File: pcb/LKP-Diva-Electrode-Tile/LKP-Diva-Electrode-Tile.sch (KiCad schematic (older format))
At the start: 19 parts, among them J1 Intercon, J10 Electrode 1, J11 Electrode 3, J12 Electrode 5, J13 Electrode 7, J14 Electrode 9, J15 Electrode 11, J16 Electrode 13, J17 Electrode 15, J2 Electrode 0, J3 Electrode 2, J4 Electrode 4, J5 Electrode 6, J6 Electrode 8, J7 Electrode 10, J8 Electrode 12, J9 Electrode 14

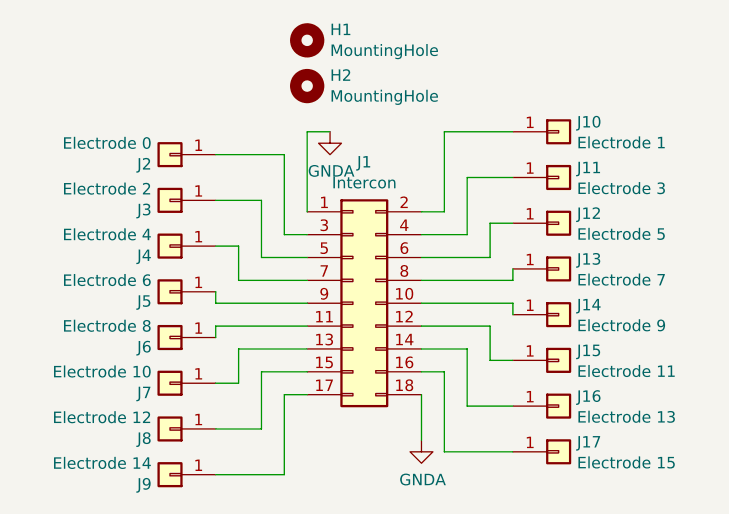
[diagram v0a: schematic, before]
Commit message: Fix sensor topology
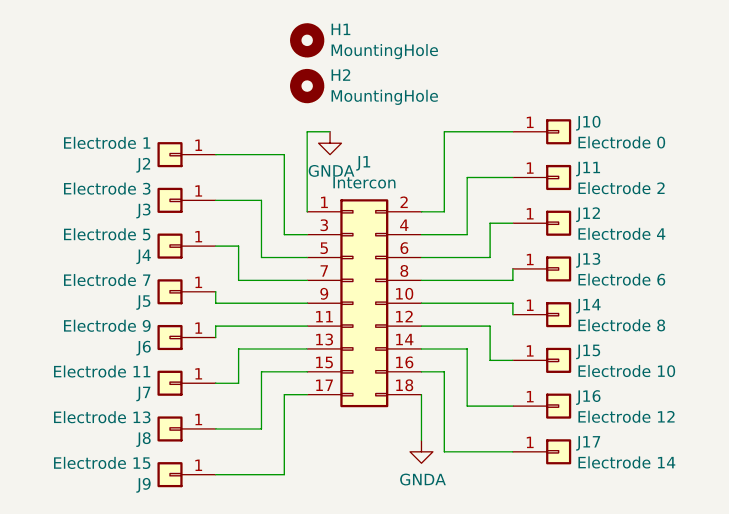
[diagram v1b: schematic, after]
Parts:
- J10: value Electrode 1 -> Electrode 0
- J11: value Electrode 3 -> Electrode 2
- J12: value Electrode 5 -> Electrode 4
- J13: value Electrode 7 -> Electrode 6
- J14: value Electrode 9 -> Electrode 8
- J15: value Electrode 11 -> Electrode 10
- J16: value Electrode 13 -> Electrode 12
- J17: value Electrode 15 -> Electrode 14
- J2: value Electrode 0 -> Electrode 1
- J3: value Electrode 2 -> Electrode 3
- J4: value Electrode 4 -> Electrode 5
- J5: value Electrode 6 -> Electrode 7
- J6: value Electrode 8 -> Electrode 9
- J7: value Electrode 10 -> Electrode 11
- J8: value Electrode 12 -> Electrode 13
- J9: value Electrode 14 -> Electrode 15
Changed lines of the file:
@@
 P 6900 3700
 F 0 "J10" H 6980 3742 50  0000 L CNN
-F 1 "Electrode 1" H 6980 3651 50  0000 L CNN
+F 1 "Electrode 0" H 6980 3651 50  0000 L CNN
 F 2 "private:CapSense_Electrode_14x38mm" H 6900 3700 50  0001 C CNN
 F 3 "~" H 6900 3700 50  0001 C CNN
@@
 P 6900 3900
 F 0 "J11" H 6980 3942 50  0000 L CNN
-F 1 "Electrode 3" H 6980 3851 50  0000 L CNN
+F 1 "Electrode 2" H 6980 3851 50  0000 L CNN
 F 2 "private:CapSense_Electrode_14x38mm" H 6900 3900 50  0001 C CNN
 F 3 "~" H 6900 3900 50  0001 C CNN
@@
 P 6900 4100
 F 0 "J12" H 6980 4142 50  0000 L CNN
-F 1 "Electrode 5" H 6980 4051 50  0000 L CNN
+F 1 "Electrode 4" H 6980 4051 50  0000 L CNN
 F 2 "private:CapSense_Electrode_14x38mm" H 6900 4100 50  0001 C CNN
 F 3 "~" H 6900 4100 50  0001 C CNN
@@
 P 6900 4300
 F 0 "J13" H 6980 4342 50  0000 L CNN
-F 1 "Electrode 7" H 6980 4251 50  0000 L CNN
+F 1 "Electrode 6" H 6980 4251 50  0000 L CNN
 F 2 "private:CapSense_Electrode_14x38mm" H 6900 4300 50  0001 C CNN
 F 3 "~" H 6900 4300 50  0001 C CNN
@@
 P 6900 4500
 F 0 "J14" H 6980 4542 50  0000 L CNN
-F 1 "Electrode 9" H 6980 4451 50  0000 L CNN
+F 1 "Electrode 8" H 6980 4451 50  0000 L CNN
 F 2 "private:CapSense_Electrode_14x38mm" H 6900 4500 50  0001 C CNN
 F 3 "~" H 6900 4500 50  0001 C CNN
@@
 P 6900 4700
 F 0 "J15" H 6980 4742 50  0000 L CNN
-F 1 "Electrode 11" H 6980 4651 50  0000 L CNN
+F 1 "Electrode 10" H 6980 4651 50  0000 L CNN
 F 2 "private:CapSense_Electrode_14x38mm" H 6900 4700 50  0001 C CNN
 F 3 "~" H 6900 4700 50  0001 C CNN
@@
 P 6900 4900
 F 0 "J16" H 6980 4942 50  0000 L CNN
-F 1 "Electrode 13" H 6980 4851 50  0000 L CNN
+F 1 "Electrode 12" H 6980 4851 50  0000 L CNN
 F 2 "private:CapSense_Electrode_14x38mm" H 6900 4900 50  0001 C CNN
 F 3 "~" H 6900 4900 50  0001 C CNN
@@
 P 6900 5100
 F 0 "J17" H 6980 5142 50  0000 L CNN
-F 1 "Electrode 15" H 6980 5051 50  0000 L CNN
+F 1 "Electrode 14" H 6980 5051 50  0000 L CNN
 F 2 "private:CapSense_Electrode_14x38mm" H 6900 5100 50  0001 C CNN
 F 3 "~" H 6900 5100 50  0001 C CNN
@@
 P 5200 4800
 F 0 "J7" H 5280 4842 50  0000 L CNN
-F 1 "Electrode 10" H 5280 4751 50  0000 L CNN
+F 1 "Electrode 11" H 5280 4751 50  0000 L CNN
 F 2 "private:CapSense_Electrode_14x38mm" H 5200 4800 50  0001 C CNN
 F 3 "~" H 5200 4800 50  0001 C CNN
@@
 P 5200 5200
 F 0 "J9" H 5280 5242 50  0000 L CNN
-F 1 "Electrode 14" H 5280 5151 50  0000 L CNN
+F 1 "Electrode 15" H 5280 5151 50  0000 L CNN
 F 2 "private:CapSense_Electrode_14x38mm" H 5200 5200 50  0001 C CNN
 F 3 "~" H 5200 5200 50  0001 C CNN
@@
 P 5200 4000
 F 0 "J3" H 5280 4042 50  0000 L CNN
-F 1 "Electrode 2" H 5280 3951 50  0000 L CNN
+F 1 "Electrode 3" H 5280 3951 50  0000 L CNN
 F 2 "private:CapSense_Electrode_14x38mm" H 5200 4000 50  0001 C CNN
 F 3 "~" H 5200 4000 50  0001 C CNN
@@
 P 5200 4400
 F 0 "J5" H 5280 4442 50  0000 L CNN
-F 1 "Electrode 6" H 5280 4351 50  0000 L CNN
+F 1 "Electrode 7" H 5280 4351 50  0000 L CNN
 F 2 "private:CapSense_Electrode_14x38mm" H 5200 4400 50  0001 C CNN
 F 3 "~" H 5200 4400 50  0001 C CNN
@@
 P 5200 4600
 F 0 "J6" H 5280 4642 50  0000 L CNN
-F 1 "Electrode 8" H 5280 4551 50  0000 L CNN
+F 1 "Electrode 9" H 5280 4551 50  0000 L CNN
 F 2 "private:CapSense_Electrode_14x38mm" H 5200 4600 50  0001 C CNN
 F 3 "~" H 5200 4600 50  0001 C CNN
@@
 P 5200 3800
 F 0 "J2" H 5280 3842 50  0000 L CNN
-F 1 "Electrode 0" H 5280 3751 50  0000 L CNN
+F 1 "Electrode 1" H 5280 3751 50  0000 L CNN
 F 2 "private:CapSense_Electrode_14x38mm" H 5200 3800 50  0001 C CNN
 F 3 "~" H 5200 3800 50  0001 C CNN
@@
 P 5200 5000
 F 0 "J8" H 5280 5042 50  0000 L CNN
-F 1 "Electrode 12" H 5280 4951 50  0000 L CNN
+F 1 "Electrode 13" H 5280 4951 50  0000 L CNN
 F 2 "private:CapSense_Electrode_14x38mm" H 5200 5000 50  0001 C CNN
 F 3 "~" H 5200 5000 50  0001 C CNN
@@
 P 5200 4200
 F 0 "J4" H 5280 4242 50  0000 L CNN
-F 1 "Electrode 4" H 5280 4151 50  0000 L CNN
+F 1 "Electrode 5" H 5280 4151 50  0000 L CNN
 F 2 "private:CapSense_Electrode_14x38mm" H 5200 4200 50  0001 C CNN
 F 3 "~" H 5200 4200 50  0001 C CNN
